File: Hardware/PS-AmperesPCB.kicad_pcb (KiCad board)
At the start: 2 copper layers, 81.8 x 95.6 mm, 160 parts, among them IC1 SN74AHC1G32DBVR, IC2 INA241A4IDR, IC3 AMC1350DWVR, IC4 TLV9002QDRQ1, IC5 LM76202QPWPRQ1, J1 PeripheralCAN, J2 PeripheralCAN, J3 SWD, J4 Conn_01x02_Pin, J5 USB4120-03-C, J6 Scrut Conn, SW1 RST, SW2 BOOT, SW3 Scrut Select, U1 LT1963AEST-3.3#TRPBF, U2 TPS5405DR, U3 TPS2115ADRBR, U4 LT1963AEST-3.3#TRPBF, U5 STM32L431CBTx, U6 TCAN337, U7 CDSOT23-T24CAN, U8 CP2102N-A02-GQFN24, U9 REF35125QDBVR, Y1 8M

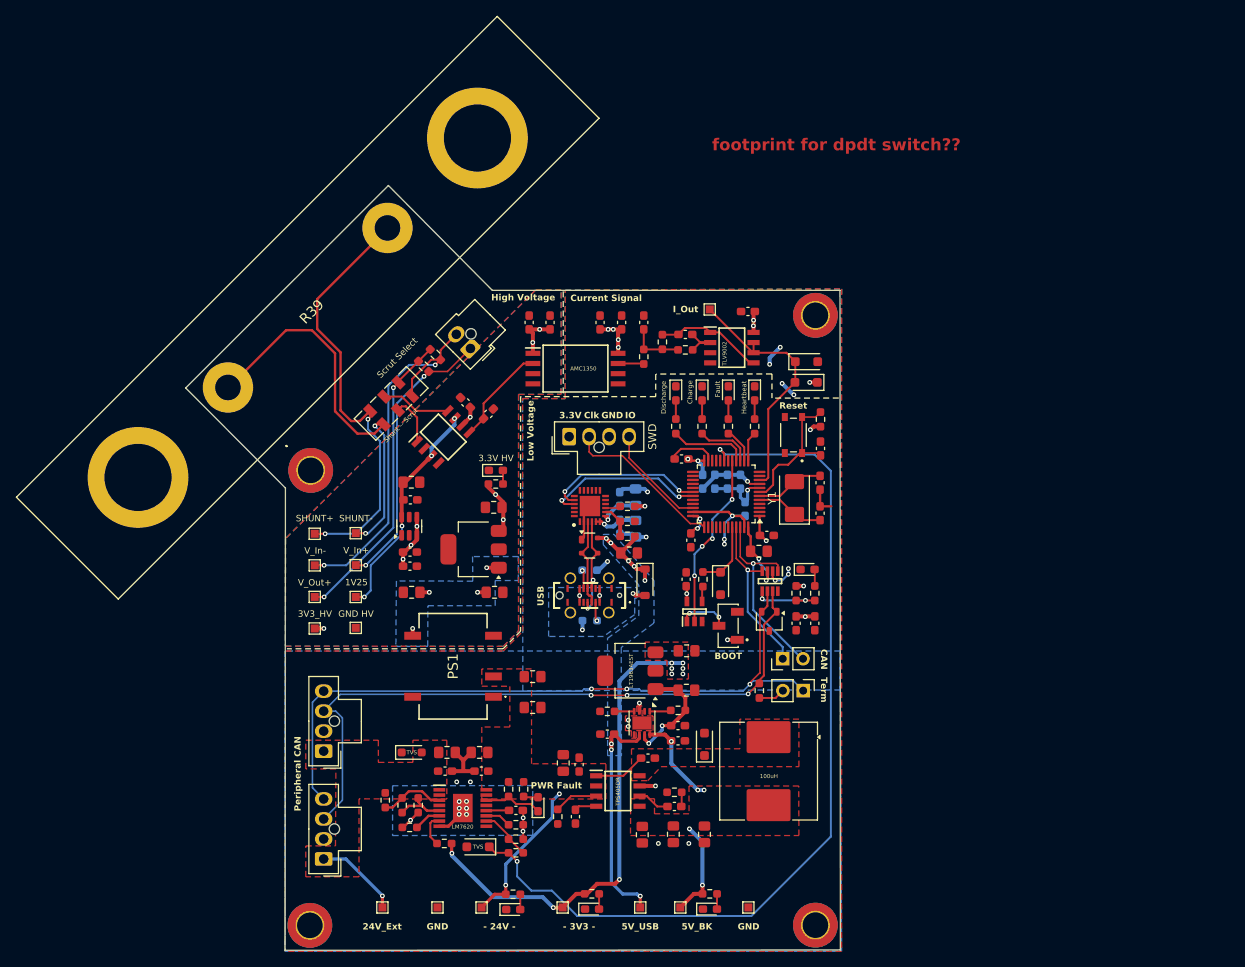
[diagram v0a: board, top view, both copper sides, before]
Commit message: more silkscreen, addressed some comments
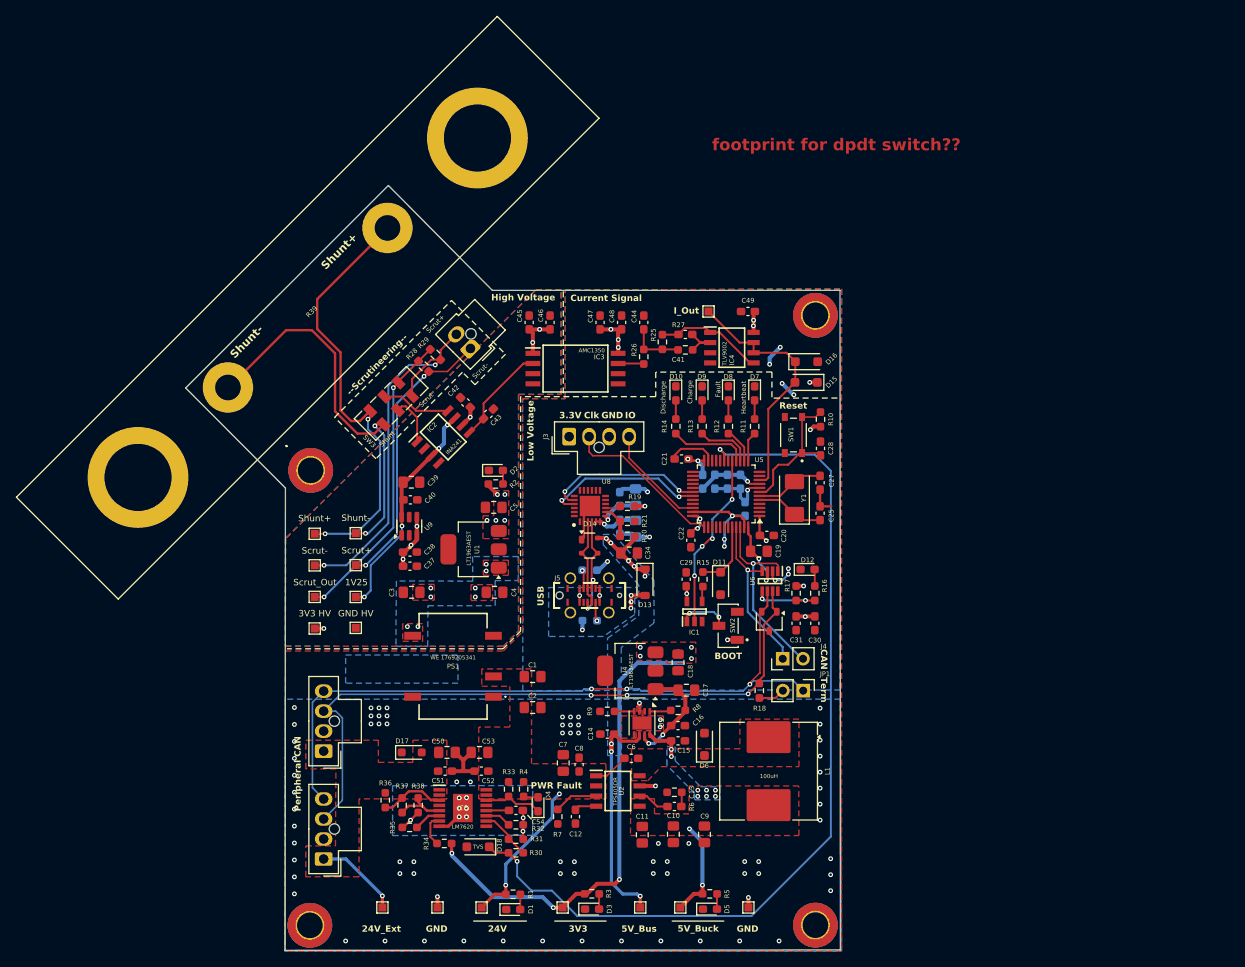
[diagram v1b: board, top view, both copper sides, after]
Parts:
- added LOGO2: Dr. Hallock, UTSVT_Logos:Hallock_Image_Tiny, B.Cu at (129.0, 62.8)
- IC1: value SN74AHC1G32DBVR -> SOT95P280X145-5N
- IC3: value AMC1350DWVR -> SOIC127P1150X280-8N
- IC4: value TLV9002QDRQ1 -> SOIC127P600X175-8N
- LOGO1: moved to B.Cu
- TP3: value - 24V - -> 24V
- TP5: value - 3V3 - -> 3V3
- moved LOGO1 52.9 mm to (137.4, 105.2), turned to 180 degrees
- moved C6 2.08 mm to (166.2, 116.4)
- moved C18 1.80 mm to (172.0, 104.4), turned to -90 degrees
- moved TP1 0.30 mm to (175.8, 60.6), turned to 0 degrees
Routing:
- net +5V_BUCK: track 23.5 -> 17.3 mm, vias 5 -> 10
- net +3.3V HV: track 23.4 -> 18.4 mm, vias 9 -> 12
- net +5V HV: track 4.70 -> 0.00 mm, vias 4 -> 8
- net GND: track 56.5 -> 60.6 mm, vias 22 -> 93
- net Net-(U2-BOOT): track 6.52 -> 4.43 mm
- net /USB/VBUS_IN: track 5.05 -> 6.80 mm, vias 3 -> 5
- net +3.3V: vias 31 -> 28
- added copper zone on B.Cu, net (none)
- added copper zone on F.Cu, net +3.3V HV
- added copper zone on F.Cu, net +5V HV
- added copper zone on B.Cu, net +5V_BUCK
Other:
- board text added: "--Scrutineering--"
- board text added: "24V"
- board text added: "24V_Ext"
- board text added: "3V3"
- board text added: "3V3 HV"
- board text added: "5V_Buck"
- board text added: "5V_Bus"
- board text added: "Charge"
- board text added: "Discharge"
- board text added: "Fault"
- board text added: "GND HV"
- board text added: "Heartbeat"
- board text added: "INA241"
- board text added: "I_Out"
- board text added: "Michael Adeluyi - Amperes RevB"
- board text added: "Scrut"
- board text added: "Scrut+"
- board text added: "Scrut-"
- board text added: "Scrut_Out"
- board text added: "Shunt"
- board text added: "Shunt+"
- board text added: "Shunt-"
- board text added: "WE 1769205341"
- board text removed: "Shunt -- Scrut"

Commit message: more comments addressed
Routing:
- net /Current Sense/Scrut-: track 47.1 -> 42.6 mm
- net /USB/VBUS_IN: track 6.80 -> 10.6 mm, vias 5 -> 7
- net /Current Sense/SHUNT+: track 55.0 -> 52.2 mm
- net +3.3V HV: track 18.4 -> 16.0 mm
- net /Current Sense/SHUNT-: track 50.0 -> 47.8 mm
- net GND: track 60.6 -> 61.8 mm, vias 93 -> 94
- net +5V_VBUS: track 40.7 -> 39.6 mm
- net +24V_Ext: track 10.7 -> 9.85 mm
- net +3.3V: track 110.3 -> 110.0 mm, vias 28 -> 27
- net /MCU/NRST: vias 0 -> 2
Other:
- board size 81.8 x 95.6 mm -> 80.6 x 94.4 mm
- board text added: "- add remaining 3d models - verify cots parts"
- board text added: "Scrutineering"
- board text removed: "--Scrutineering--"
- board text removed: "footprint for dpdt switch??"

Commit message: drc drc
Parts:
- moved C19 1.20 mm to (183.3, 90.4)
- moved D13 0.90 mm to (167.9, 95.3)
- moved U6 0.60 mm to (183.5, 94.9)
- moved R19 0.50 mm to (165.7, 84.4)
- moved R21 0.32 mm to (165.7, 86.5)
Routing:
- net GND: track 61.8 -> 60.1 mm
- net /USB/VBUS_IN: track 10.6 -> 9.06 mm, vias 7 -> 5
- net /CAN/Fault: track 8.78 -> 10.0 mm
- net +3.3V: track 110.0 -> 111.2 mm
- net /CAN_LOW: track 88.4 -> 87.8 mm
- net /CAN_HIGH: track 85.0 -> 84.4 mm
- net +5V_VBUS: track 39.6 -> 39.3 mm, vias 8 -> 7
- net /MCU/SWDIO: vias 0 -> 2
- net /MCU/BOOT0: vias 0 -> 1

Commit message: updated some component part nums
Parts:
- IC1: value SOT95P280X145-5N -> SN74AHC1G32DBVR
- IC3: value SOIC127P1150X280-8N -> AMC1350DWVR
- IC4: value SOIC127P600X175-8N -> TLV9002QDRQ1
- R10: value 10K -> 10k
- TP1: value I_Out -> TP_Current

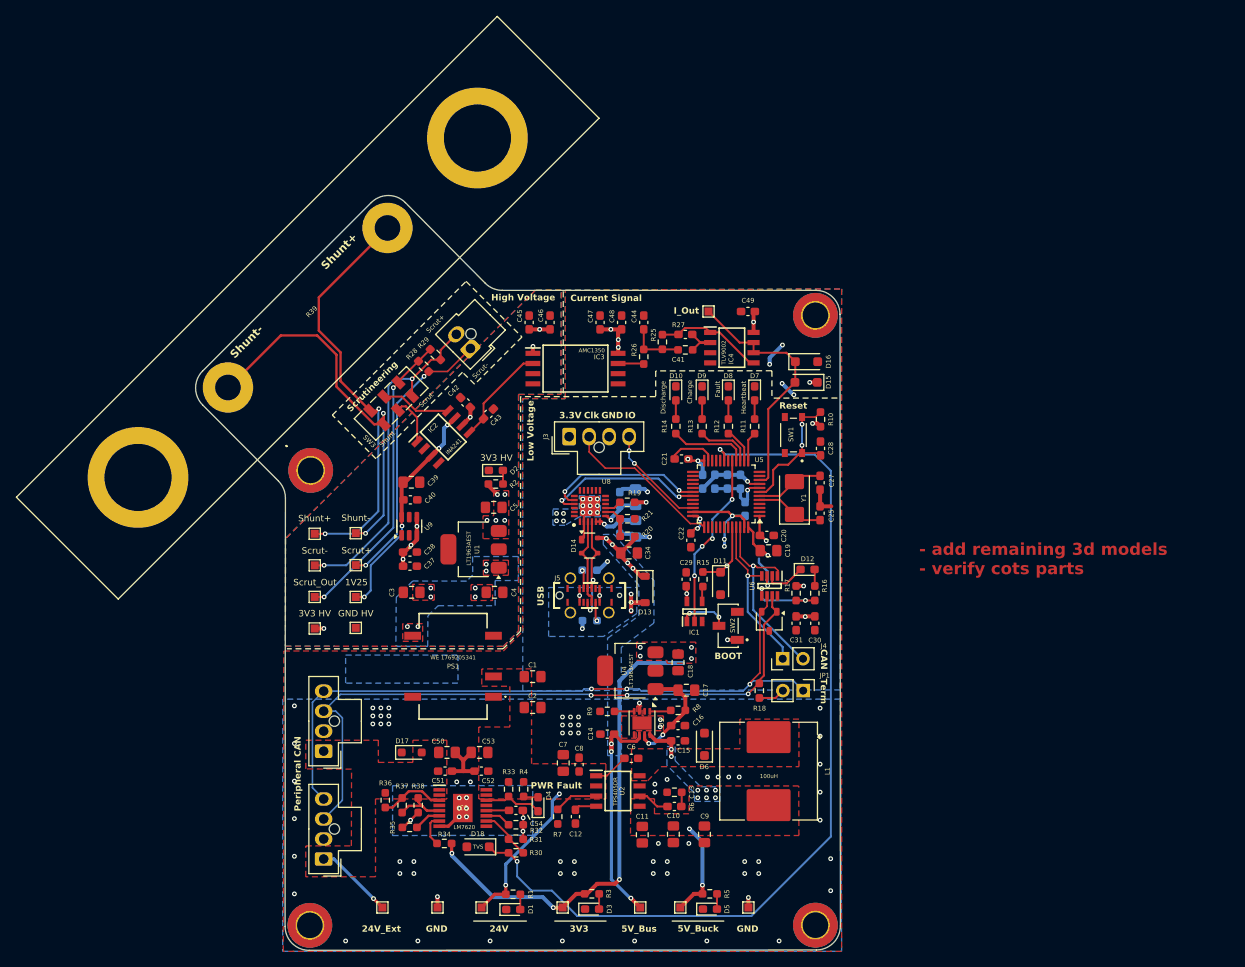
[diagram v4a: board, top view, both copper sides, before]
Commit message: new dpdt switch, layout done
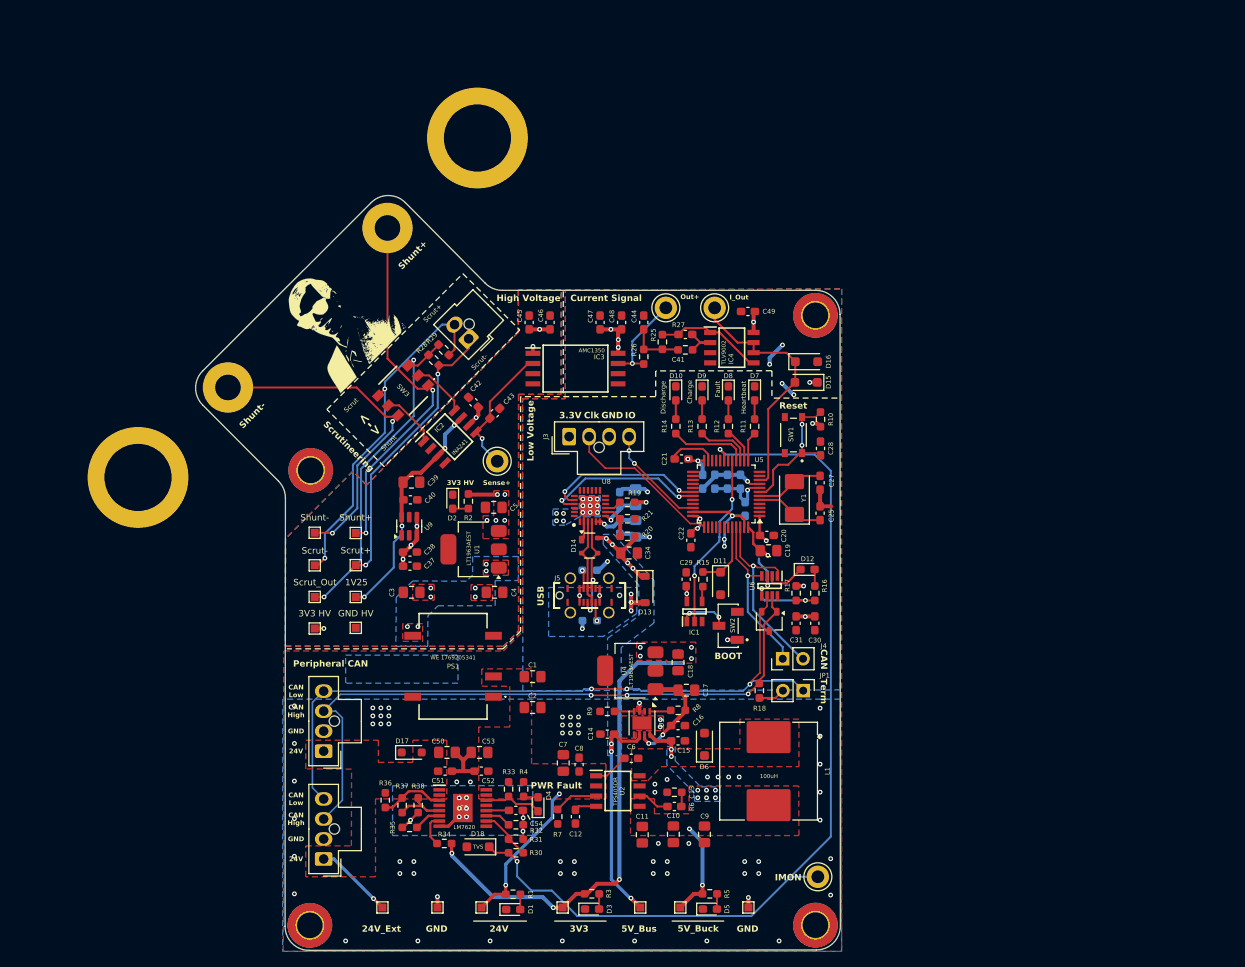
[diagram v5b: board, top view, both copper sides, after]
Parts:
- added TP17: Sense+, TestPoint:TestPoint_Keystone_5005-5009_Compact, F.Cu at (149.4, 79.3)
- added TP18: Out+, TestPoint:TestPoint_Keystone_5005-5009_Compact, F.Cu at (170.5, 60.1)
- added TP19: IMON, TestPoint:TestPoint_Keystone_5005-5009_Compact, F.Cu at (189.5, 131.2)
- LOGO2: moved to F.Cu
- R31: value 19K -> 19k
- R39: moved to B.Cu
- SW3: footprint Button_Switch_SMD:SW_DPDT_CK_JS202011JCQN -> Parts:CAS220TB
- TP1: footprint TestPoint:TestPoint_Pad_1.0x1.0mm -> TestPoint:TestPoint_Keystone_5005-5009_Compact
- moved D2 6.66 mm to (143.8, 84.3), turned to -90 degrees
- moved TP10 5.13 mm to (131.7, 88.2)
- moved TP11 5.13 mm to (126.6, 88.2)
- moved R2 4.04 mm to (145.8, 84.3), turned to -90 degrees
- moved SW3 2.21 mm to (137.6, 70.4), turned to 135 degrees
- moved R28 1.48 mm to (141.5, 66.6)
- moved J6 1.24 mm to (145.8, 64.0)
- moved R29 1.19 mm to (142.7, 65.3)
- moved C42 0.99 mm to (146.4, 71.9)
- moved TP1 0.89 mm to (176.6, 60.1)
- moved LOGO2 0.81 mm to (128.7, 62.1), turned to 45 degrees
- moved IC2 0.81 mm to (143.5, 76.2)
- moved C43 0.79 mm to (149.1, 73.3)
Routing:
- net /Current Sense/OUT+: track 3.24 -> 11.9 mm, vias 0 -> 1
- net /Current Sense/SHUNT+: track 52.2 -> 46.6 mm
- net /Current Sense/SHUNT-: track 47.8 -> 43.2 mm
- net /Current Sense/SENSE+: track 12.6 -> 16.6 mm, vias 0 -> 1
- net /Current Sense/Scrut_Out: track 37.5 -> 41.3 mm
- net /MCU/ADC1_IN16: track 113.8 -> 117.5 mm
- net +3.3V HV: track 16.0 -> 18.0 mm
- net /Current Sense/INPUT+: track 8.67 -> 7.10 mm
- net /Current Sense/Scrut-: track 42.6 -> 43.7 mm
- net /Current Sense/INPUT-: track 6.17 -> 7.14 mm
- net /Current Sense/Scrut+: track 35.1 -> 35.8 mm
- net /MCU/Boot_GPIO: track 22.2 -> 22.1 mm, vias 4 -> 2
- net /MCU/BOOT0: vias 1 -> 0
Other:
- board text added: "<->"
- board text added: "CAN High"
- board text added: "CAN Low"
- board text added: "IMON"
- board text added: "Michael Adeluyi - Amperes RevB - October 2025"
- board text added: "Out+"
- board text added: "Sense+"
- board text removed: "- add remaining 3d models - verify cots parts"
- board text removed: "Michael Adeluyi - Amperes RevB"
